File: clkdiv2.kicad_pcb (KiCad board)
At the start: 2 copper layers, 11 parts, among them J1 Conn_02x05_Odd_Even

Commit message: pcb ready for v0 manu
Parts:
- added C3: 100n, Capacitor_SMD:C_0805_2012Metric, B.Cu at (153.9, 73.9)
- added C4: 47n box, Capacitor_THT:C_Rect_L7.2mm_W2.5mm_P5.00mm_FKS2_FKP2_MKS2_MKP2, B.Cu at (118.6, 56.0)
- added D10: LED_GREEN, LED_THT:LED_D3.0mm, B.Cu at (132.8, 80.3)
- added D3: 1N4148, Diode_SMD:D_SOD-323_HandSoldering, B.Cu at (124.1, 46.1)
- added D4: 1N4148, Diode_SMD:D_SOD-323_HandSoldering, B.Cu at (124.1, 51.2)
- added D5: 1N4148, Diode_SMD:D_SOD-323_HandSoldering, B.Cu at (133.2, 46.1)
- added D6: 1N4148, Diode_SMD:D_SOD-323_HandSoldering, B.Cu at (144.3, 66.3)
- added D7: 1N4148, Diode_SMD:D_SOD-323_HandSoldering, B.Cu at (152.1, 81.3)
- added D8: 1N4148, Diode_SMD:D_SOD-323_HandSoldering, B.Cu at (159.0, 74.8)
- added D9: Zener 5.1V, Diode_SMD:D_MiniMELF, B.Cu at (133.9, 71.1)
- added H5: in, Eurorack:Mech-AudioJack-Hole-Input-Clock, F.Cu at (121.9, 102.7)
- added H6: reset, Eurorack:Mech-AudioJack-Hole-Input-Gate, F.Cu at (121.9, 113.9)
- added H7: out, Eurorack:Mech-AudioJack-Hole-Output-Gate, F.Cu at (134.1, 102.7)
- added H8: step, Eurorack:Mech-MRK-Hole, F.Cu at (149.9, 108.3)
- added H9: led, Eurorack:Mech-LED-Hole-3mm-Bezel, F.Cu at (134.1, 113.9)
- added J10: Conn_01x03_Pin, Connector_PinHeader_2.54mm:PinHeader_1x03_P2.54mm_Vertical, B.Cu at (114.0, 71.6)
- added J2: AudioJack2_SwitchT, Eurorack:AudioJack2_Tayda_A-2566, F.Cu at (121.9, 69.1)
- added J3: AudioJack2_SwitchT, Eurorack:AudioJack2_Tayda_A-2566, F.Cu at (121.9, 80.3)
- added J4: AudioJack2_SwitchT, Eurorack:AudioJack2_Tayda_A-2566, F.Cu at (134.1, 69.1)
- added J5: Conn_01x03_Socket, Connector_PinSocket_2.54mm:PinSocket_1x03_P2.54mm_Vertical, F.Cu at (160.3, 53.7)
- added J6: Conn_01x03_Pin, Connector_PinHeader_2.54mm:PinHeader_1x03_P2.54mm_Vertical, B.Cu at (160.3, 78.8)
- added J7: Conn_01x03_Socket, Connector_PinSocket_2.54mm:PinSocket_1x03_P2.54mm_Vertical, F.Cu at (160.3, 40.8)
- added J8: Conn_01x03_Pin, Connector_PinHeader_2.54mm:PinHeader_1x03_P2.54mm_Vertical, B.Cu at (160.3, 65.8)
- added J9: Conn_01x03_Socket, Connector_PinSocket_2.54mm:PinSocket_1x03_P2.54mm_Vertical, F.Cu at (114.0, 46.6)
- added Q1: BC847, Package_SO:TSOP-6_1.65x3.05mm_P0.95mm, B.Cu at (128.2, 46.1)
- added Q2: BC847, Package_SO:TSOP-6_1.65x3.05mm_P0.95mm, B.Cu at (128.2, 51.2)
- added Q3: BC847, Package_SO:TSOP-6_1.65x3.05mm_P0.95mm, B.Cu at (138.9, 77.0)
- added R10: 10K, Resistor_SMD:R_0805_2012Metric, B.Cu at (138.6, 55.5)
- added R11: 220K, Resistor_SMD:R_0805_2012Metric, B.Cu at (128.2, 55.7)
- added R12: 22K, Resistor_SMD:R_0805_2012Metric, B.Cu at (135.0, 50.9)
- added R13: 1K, Resistor_SMD:R_0805_2012Metric, B.Cu at (133.2, 41.8)
- added R14: 22K, Resistor_SMD:R_0805_2012Metric, B.Cu at (156.5, 82.3)
- added R15: 4.7K, Resistor_SMD:R_0805_2012Metric, B.Cu at (141.5, 70.6)
- added R16: 220K, Resistor_SMD:R_0805_2012Metric, B.Cu at (142.5, 78.7)
- added R17: 120K, Resistor_SMD:R_0805_2012Metric, B.Cu at (134.9, 68.3)
- added R18: 1K, Resistor_SMD:R_0805_2012Metric, B.Cu at (138.7, 72.9)
- added R19: 1K, Resistor_SMD:R_0805_2012Metric, B.Cu at (131.8, 77.0)
- added R20: 10, Resistor_SMD:R_0805_2012Metric, B.Cu at (138.6, 47.9)
- added R3: 1M, Resistor_SMD:R_0805_2012Metric, B.Cu at (118.8, 43.5)
- added R4: 1.2M, Resistor_SMD:R_0805_2012Metric, B.Cu at (119.5, 47.1)
- added R5: 22K, Resistor_SMD:R_0805_2012Metric, B.Cu at (138.6, 50.4)
- added R6: 22K, Resistor_SMD:R_0805_2012Metric, B.Cu at (138.6, 52.9)
- added R7: 220, Resistor_SMD:R_0805_2012Metric, B.Cu at (127.7, 41.8)
- added R8: 100K, Resistor_SMD:R_0805_2012Metric, B.Cu at (119.5, 49.9)
- added R9: 1M, Resistor_SMD:R_0805_2012Metric, B.Cu at (131.7, 50.9)
- added SW1: SW_Rotary12, Eurorack:Switch_Rotary_NKK_MRK_112, F.Cu at (149.9, 74.7)
- added U1: 4017, Package_SO:TSSOP-16_4.4x5mm_P0.65mm, B.Cu at (149.9, 74.7)
- moved H3 156.0 mm to (157.4, 125.2)
- moved H2 139.3 mm to (157.4, 91.5)
- moved H4 123.9 mm to (116.9, 125.2)
- moved H1 109.3 mm to (116.9, 91.5)
- moved J1 66.9 mm to (151.4, 54.6), turned to 0 degrees
- moved R2 54.2 mm to (145.1, 54.0), turned to 0 degrees
- moved C1 54.2 mm to (144.5, 43.2), turned to 90 degrees
- moved R1 53.7 mm to (145.1, 51.5), turned to 0 degrees
- moved D1 53.4 mm to (143.8, 57.8), turned to -90 degrees
- moved D2 51.4 mm to (143.8, 47.7), turned to -90 degrees
- moved C2 45.2 mm to (138.8, 40.7), turned to -90 degrees
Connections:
- C2 pad 2: -12V -> /V_LED
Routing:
- net +12V: track 14.0 -> 71.4 mm, vias 0 -> 1
- net /_IN: track 0.00 -> 45.4 mm, vias 0 -> 1
- net GND: track 0.00 -> 40.1 mm, vias 0 -> 6
- net /V_LED: track 0.00 -> 37.4 mm
- net /GND': track 0.00 -> 35.0 mm, vias 0 -> 1
- net /_RST: track 0.00 -> 30.6 mm
- net /_IN': track 0.00 -> 29.4 mm, vias 0 -> 1
- net /V_LED': track 0.00 -> 29.0 mm
- net Net-(Q2A-C1): track 0.00 -> 27.6 mm
- net Net-(D6-A): track 0.00 -> 27.1 mm, vias 0 -> 2
- net Net-(U1-Q5): track 0.00 -> 25.8 mm
- net Net-(U1-Q7): track 0.00 -> 21.5 mm
- net /_RST': track 0.00 -> 19.9 mm, vias 0 -> 1
- net /12V': track 0.00 -> 16.7 mm, vias 0 -> 1
- net /RST': track 0.00 -> 15.6 mm
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- added copper zone on B.Cu, net /FACE
- added copper zone on F.Cu, net /FACE
- added copper zone on B.Cu, net /GND'
- added copper zone on F.Cu, net /GND'
- added copper zone on B.Cu, net GND
- added copper zone on F.Cu, net GND
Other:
- board outline added: 50.5 x 89.7 mm
- board text added: "1"
- board text added: "10"
- board text added: "2"
- board text added: "3"
- board text added: "4"
- board text added: "5"
- board text added: "6"
- board text added: "7"
- board text added: "8"
- board text added: "9"
- board text added: "clock/n"
- board text added: "in"
- board text added: "n"
- board text added: "out"
- board text added: "reset"
- board text added: "thismatters/clkdiv2/v0"

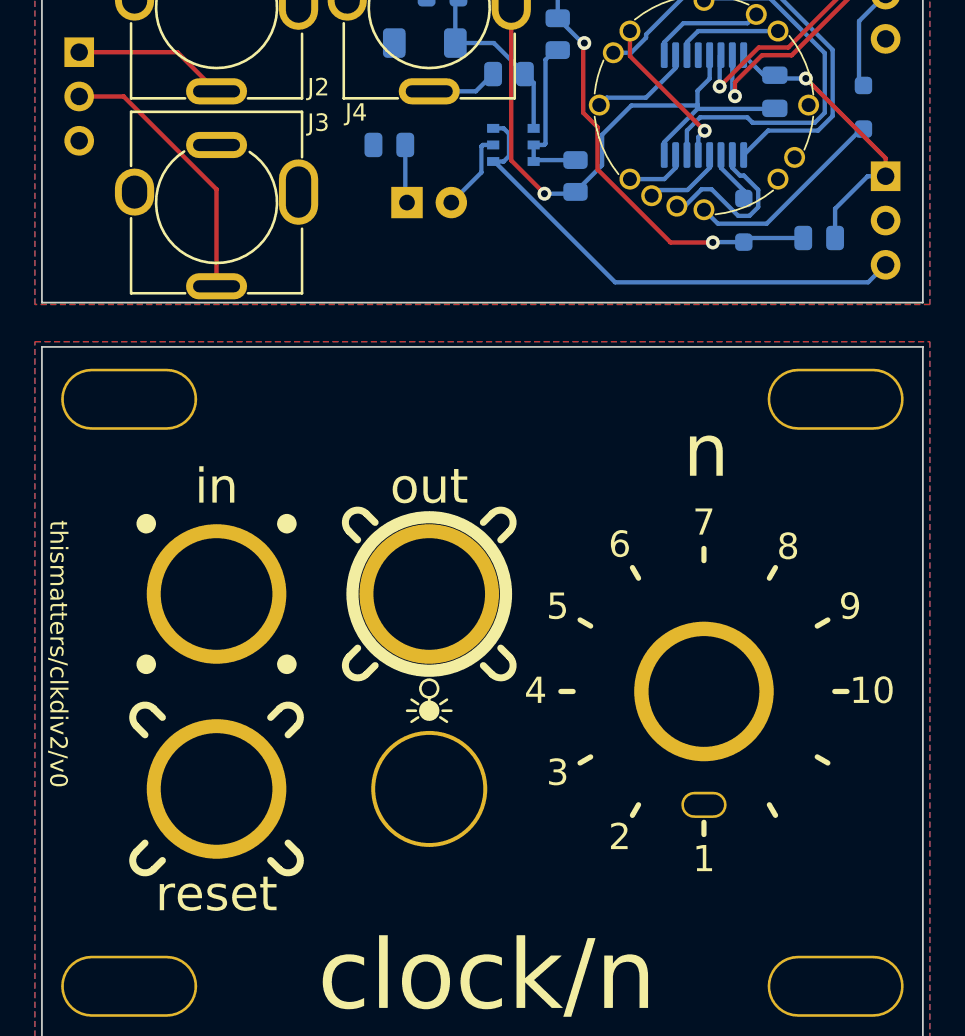
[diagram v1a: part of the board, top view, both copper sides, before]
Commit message: pcb ready for v0a manu
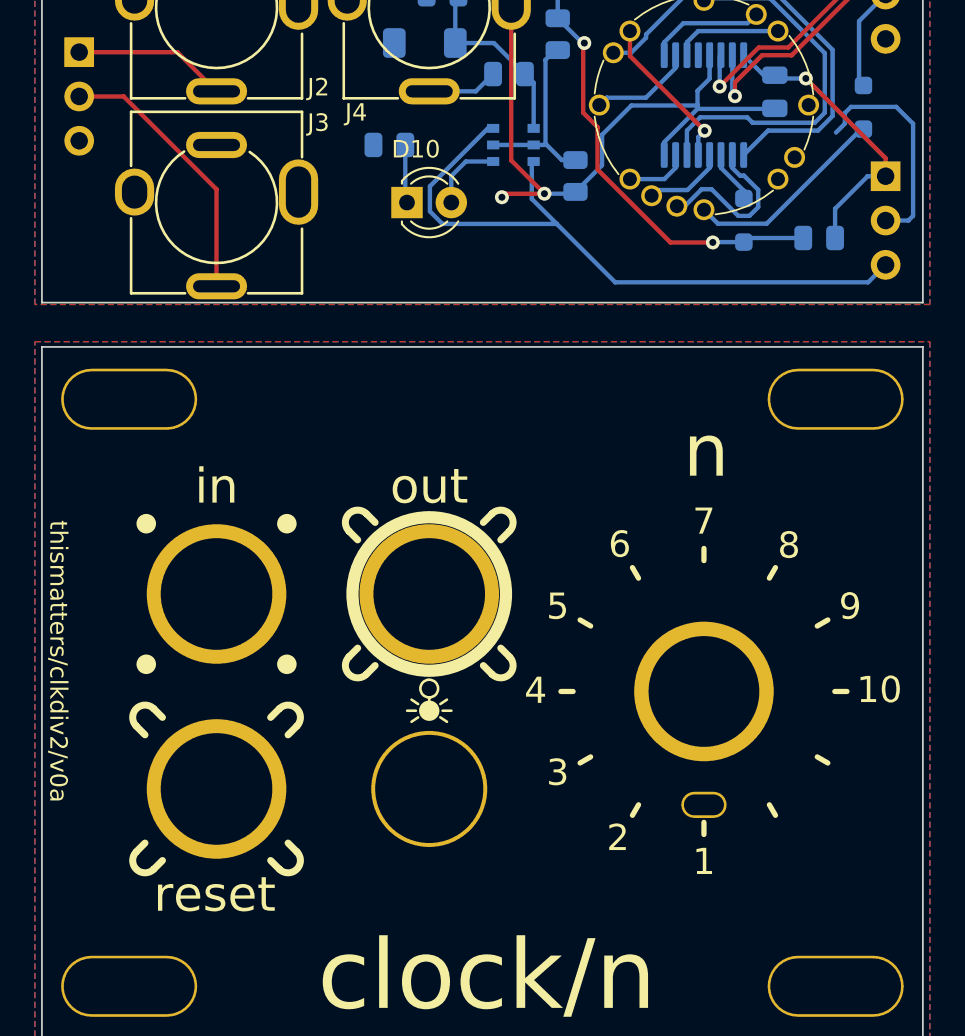
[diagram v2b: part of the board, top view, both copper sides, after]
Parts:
- D10: moved to F.Cu
- Q1, Q2, Q3: value BC847 -> BCM847
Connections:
- Q3 pad 1: /V_LED' -> Net-(D10-A)
- Q3 pad 2: Net-(D10-A) -> Net-(Q3A-B1)
- Q3 pad 6: Net-(Q3A-B1) -> /V_LED'
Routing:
- net /GND': track 35.0 -> 50.3 mm, vias 1 -> 2
- net /V_LED': track 29.0 -> 38.7 mm
- net Net-(Q3A-B1): track 9.56 -> 10.7 mm
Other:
- board text added: "thismatters/clkdiv2/v0a"
- board text removed: "thismatters/clkdiv2/v0"
